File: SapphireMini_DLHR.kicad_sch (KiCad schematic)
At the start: 24 parts, among them IC201 DLHR-F50D-E1BD-C-NAV8, U201 LIS331DLHTR, U202 BMP388

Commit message: Minor changes to annotation
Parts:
- removed R203, R206: 10K, Resistor_SMD:R_0603_1608Metric, symbol Device:R_Small_US
- removed R208, R211: 4K75, Resistor_SMD:R_0603_1608Metric, symbol Device:R_Small_US
- added R209, R210: 47, Resistor_SMD:R_0603_1608Metric, symbol Device:R_Small_US
- renumbered R212 to R203, R207 to R206, R209 to R207, R210 to R208, R213 to R211
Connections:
- net I2C_SCL: now also R209.2; no longer U202.2 (SCK)
- net I2C_SDA: now also R210.2; no longer U202.4 (SDI)
- new net: R209.1, U202.2 (SCK)
- new net: R210.1, U202.4 (SDI)
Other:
- note added: "BMP390 address 0x76"
- note added: "DLHR I2C address 0x29"
- note added: "LIS331DLHTR address 0x12"

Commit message: Footprints complete. Starting layout
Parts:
- C201: MPN CGA5L1X5R1C226M160AC -> CL21A226MAYNNNE; Manufacturer TDK -> Samsung
- C202, C203, C205, C206, C207: MPN CL10B104KA8NNNC -> CL05A104KA5NNNC
- C204: MPN GRM21BR61E106MA73L -> CL21A106KAYNNNE
- FB201: footprint (none) -> Inductor_SMD:L_0201_0603Metric; MPN (none) -> BLM18AG221SN1D
- IC201: Status Trays -> (none)
- U201: footprint LGA-16_3x3x1mm_STM -> SapphineMinimal:LIS331DLHTR
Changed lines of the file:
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@@
       (effects (font (size 1.27 1.27)) hide)
     )
-    (property "MPN" "CL10B104KA8NNNC" (id 5) (at 73.66 67.31 0)
+    (property "MPN" "CL05A104KA5NNNC" (id 5) (at 73.66 67.31 0)
       (effects (font (size 1.27 1.27)) hide)
     )
@@
       (effects (font (size 1.27 1.27)) hide)
     )
-    (property "Description" "0.1 µF ±10% 25V Ceramic Capacitor X7R 0603 (1608 Metric)" (id 15) (at 73.66 67.31 0)
+    (property "Description" "0.1 µF ±10% 25V Ceramic Capacitor X5R 0402 (1005 Metric)" (id 15) (at 73.66 67.31 0)
       (effects (font (size 1.27 1.27)) hide)
     )
@@
       (effects (font (size 1.27 1.27)) hide)
     )
-    (property "MPN" "CL10B104KA8NNNC" (id 5) (at 59.69 67.31 0)
+    (property "MPN" "CL05A104KA5NNNC" (id 5) (at 59.69 67.31 0)
       (effects (font (size 1.27 1.27)) hide)
     )
@@
       (effects (font (size 1.27 1.27)) hide)
     )
-    (property "Description" "0.1 µF ±10% 25V Ceramic Capacitor X7R 0603 (1608 Metric)" (id 15) (at 59.69 67.31 0)
+    (property "Description" "0.1 µF ±10% 25V Ceramic Capacitor X5R 0402 (1005 Metric)" (id 15) (at 59.69 67.31 0)
       (effects (font (size 1.27 1.27)) hide)
     )
@@
       (effects (font (size 1.27 1.27)) hide)
     )
-    (property "MPN" "CGA5L1X5R1C226M160AC" (id 6) (at 46.99 67.31 0)
-      (effects (font (size 1.27 1.27)) hide)
-    )
-    (property "Manufacturer" "TDK" (id 7) (at 46.99 67.31 0)
+    (property "MPN" "CL21A226MAYNNNE" (id 6) (at 46.99 67.31 0)
+      (effects (font (size 1.27 1.27)) hide)
+    )
+    (property "Manufacturer" "Samsung" (id 7) (at 46.99 67.31 0)
       (effects (font (size 1.27 1.27)) hide)
     )
@@
       (effects (font (size 1.27 1.27)) hide)
     )
-    (property "Description" "22 µF ±20% 16V Ceramic Capacitor X5R 1206" (id 16) (at 46.99 67.31 0)
+    (property "Description" "22 µF ±20% 25V Ceramic Capacitor X5R 0805 (2012 Metric)" (id 16) (at 46.99 67.31 0)
       (effects (font (size 1.27 1.27)) hide)
     )
@@
       (effects (font (size 1.27 1.27)) (justify left) hide)
     )
-    (property "Description" "Board Mount Pressure Sensors Low Voltage Digital Pressure Sensor, 0.5 inH2O" (id 4) (at 121.92 59.69 0)
+    (property "Description" "SENSOR PRESSURE 0.5\" H2O 18 BIT" (id 4) (at 121.92 59.69 0)
       (effects (font (size 1.27 1.27)) (justify left) hide)
     )
@@
       (effects (font (size 1.27 1.27)) hide)
     )
-    (property "Status" "Trays" (id 19) (at 92.71 57.15 0)
+    (property "Status" "" (id 19) (at 92.71 57.15 0)
       (effects (font (size 1.27 1.27)) hide)
     )
@@
       (effects (font (size 1.27 1.27)) hide)
     )
-    (property "MPN" "CL10B104KA8NNNC" (id 5) (at 153.67 140.97 0)
+    (property "MPN" "CL05A104KA5NNNC" (id 5) (at 153.67 140.97 0)
       (effects (font (size 1.27 1.27)) hide)
     )
@@
       (effects (font (size 1.27 1.27)) hide)
     )
-    (property "Description" "0.1 µF ±10% 25V Ceramic Capacitor X7R 0603 (1608 Metric)" (id 15) (at 153.67 140.97 0)
+    (property "Description" "0.1 µF ±10% 25V Ceramic Capacitor X5R 0402 (1005 Metric)" (id 15) (at 153.67 140.97 0)
       (effects (font (size 1.27 1.27)) hide)
     )
@@
       (effects (font (size 1.524 1.524)))
     )
-    (property "Footprint" "LGA-16_3x3x1mm_STM" (id 2) (at 95.25 139.954 0)
+    (property "Footprint" "SapphineMinimal:LIS331DLHTR" (id 2) (at 95.25 139.954 0)
       (effects (font (size 1.524 1.524)) hide)
     )
@@
       (effects (font (size 1.27 1.27)) hide)
     )
-    (property "MPN" "GRM21BR61E106MA73L" (id 5) (at 142.24 140.97 0)
+    (property "MPN" "CL21A106KAYNNNE" (id 5) (at 142.24 140.97 0)
       (effects (font (size 1.27 1.27)) hide)
     )
@@
       (effects (font (size 1.27 1.27)) hide)
     )
-    (property "Description" "10 µF ±20% 25V Ceramic Capacitor X5R 0805" (id 8) (at 142.24 140.97 0)
+    (property "Description" "10 µF ±10% 25V Ceramic Capacitor X5R 0805 (2012 Metric)" (id 8) (at 142.24 140.97 0)
       (effects (font (size 1.27 1.27)) hide)
     )
@@
       (effects (font (size 1.27 1.27)) hide)
     )
-    (property "MPN" "CL10B104KA8NNNC" (id 5) (at 228.6 76.2 0)
+    (property "MPN" "CL05A104KA5NNNC" (id 5) (at 228.6 76.2 0)
       (effects (font (size 1.27 1.27)) hide)
     )
@@
       (effects (font (size 1.27 1.27)) hide)
     )
-    (property "Description" "0.1 µF ±10% 25V Ceramic Capacitor X7R 0603 (1608 Metric)" (id 15) (at 228.6 76.2 0)
+    (property "Description" "0.1 µF ±10% 25V Ceramic Capacitor X5R 0402 (1005 Metric)" (id 15) (at 228.6 76.2 0)
       (effects (font (size 1.27 1.27)) hide)
     )
@@
       (effects (font (size 1.27 1.27)) hide)
     )
-    (property "MPN" "CL10B104KA8NNNC" (id 5) (at 236.22 73.66 0)
+    (property "MPN" "CL05A104KA5NNNC" (id 5) (at 236.22 73.66 0)
       (effects (font (size 1.27 1.27)) hide)
     )
@@
       (effects (font (size 1.27 1.27)) hide)
     )
-    (property "Description" "0.1 µF ±10% 25V Ceramic Capacitor X7R 0603 (1608 Metric)" (id 15) (at 236.22 73.66 0)
+    (property "Description" "0.1 µF ±10% 25V Ceramic Capacitor X5R 0402 (1005 Metric)" (id 15) (at 236.22 73.66 0)
       (effects (font (size 1.27 1.27)) hide)
     )
@@
     (property "Reference" "FB201" (id 0) (at 65.9892 53.3486 90))
     (property "Value" "FerriteBead" (id 1) (at 65.9892 55.8855 90))
-    (property "Footprint" "" (id 2) (at 66.04 61.468 90)
+    (property "Footprint" "Inductor_SMD:L_0201_0603Metric" (id 2) (at 66.04 61.468 90)
       (effects (font (size 1.27 1.27)) hide)
     )
@@
       (effects (font (size 1.27 1.27)) hide)
     )
+    (property "Description" "220 Ohms @ 100 MHz 1 Ferrite Bead 0603 (1608 Metric) 500mA 250mOhm" (id 4) (at 66.04 59.69 0)
+      (effects (font (size 1.27 1.27)) hide)
+    )
+    (property "MPN" "BLM18AG221SN1D" (id 5) (at 66.04 59.69 0)
+      (effects (font (size 1.27 1.27)) hide)
+    )

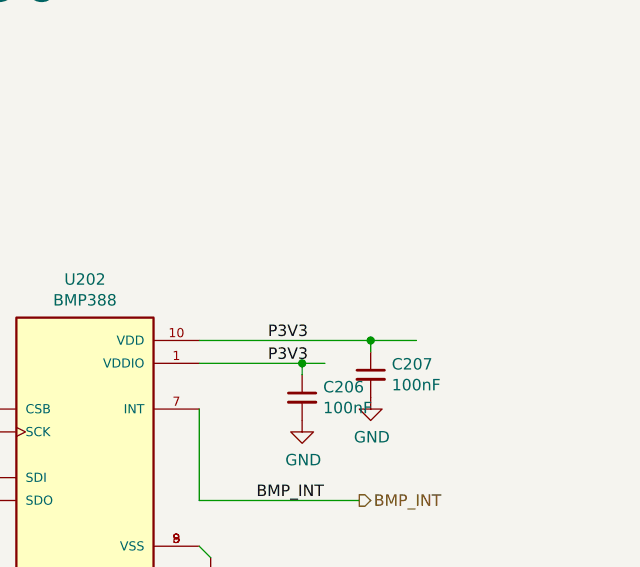
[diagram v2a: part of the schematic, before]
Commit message: replacing w/ resistor array
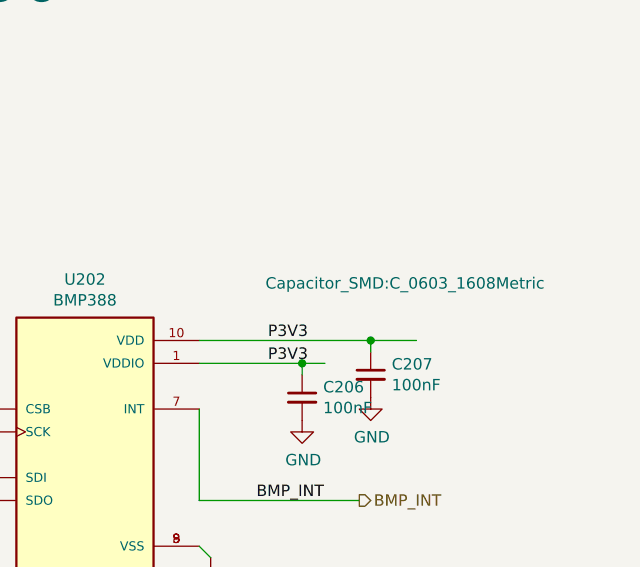
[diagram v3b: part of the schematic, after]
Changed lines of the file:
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@@
       (effects (font (size 1.27 1.27)) (justify left))
     )
-    (property "Footprint" "Capacitor_SMD:C_0603_1608Metric" (id 2) (at 236.22 73.66 0)
-      (effects (font (size 1.27 1.27)) hide)
-    )
+    (property "Footprint" "Capacitor_SMD:C_0603_1608Metric" (id 2) (at 240.03 63.5 0))
     (property "Datasheet" "~" (id 3) (at 236.22 73.66 0)
       (effects (font (size 1.27 1.27)) hide)

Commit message: Checkpoint
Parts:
- removed C204: 10uF, Capacitor_SMD:C_0805_2012Metric, symbol Device:C_Small
- removed C206: 100nF, Capacitor_SMD:C_0603_1608Metric, symbol Device:C_Small
- removed R201, R202, R203, R207, R208, R209, R210: 47, Resistor_SMD:R_0603_1608Metric, symbol Device:R_Small_US
- added R201: EXB-2HV470JV, Sapphire:EXB-2HV470JV, symbol PanasonicRA:EXB-2HV470JV
- U201: footprint SapphineMinimal:LIS331DLHTR -> Sapphire:LIS331DLHTR; DPN 497-10397-1-ND -> (none); Digi-Key_PN 497-10397-1-ND -> (none); Distributor Digikey -> (none); MPN LIS331DLHTR -> (none); Populate 0 -> (none)
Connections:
- net ACC_INT1: now also R201.5
- net ACC_INT2: now also R201.4
- net GND: now also R201.2
- net I2C_SCL: now also R201.1, R201.6
- net I2C_SDA: now also R201.3, R201.7
- net at U201.6 (SDA/SDI/SDO): now also R201.14
- net at U201.4 (SCL/SPC): now also R201.16
- net at U201.11 (INT1): now also R201.12
- net at U201.7 (SDO/SA0): now also R201.15
- net at U201.9 (INT2): now also R201.13
- net BMP_SCK: now reaches U202.2 (SCK)
- net BMP_SCK: now also R201.11
- net BMP_SDI: now reaches U202.4 (SDI)
- net BMP_SDI: now also R201.10
- no-connect marks 2 -> 4
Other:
- moved on the sheet: C205, R206

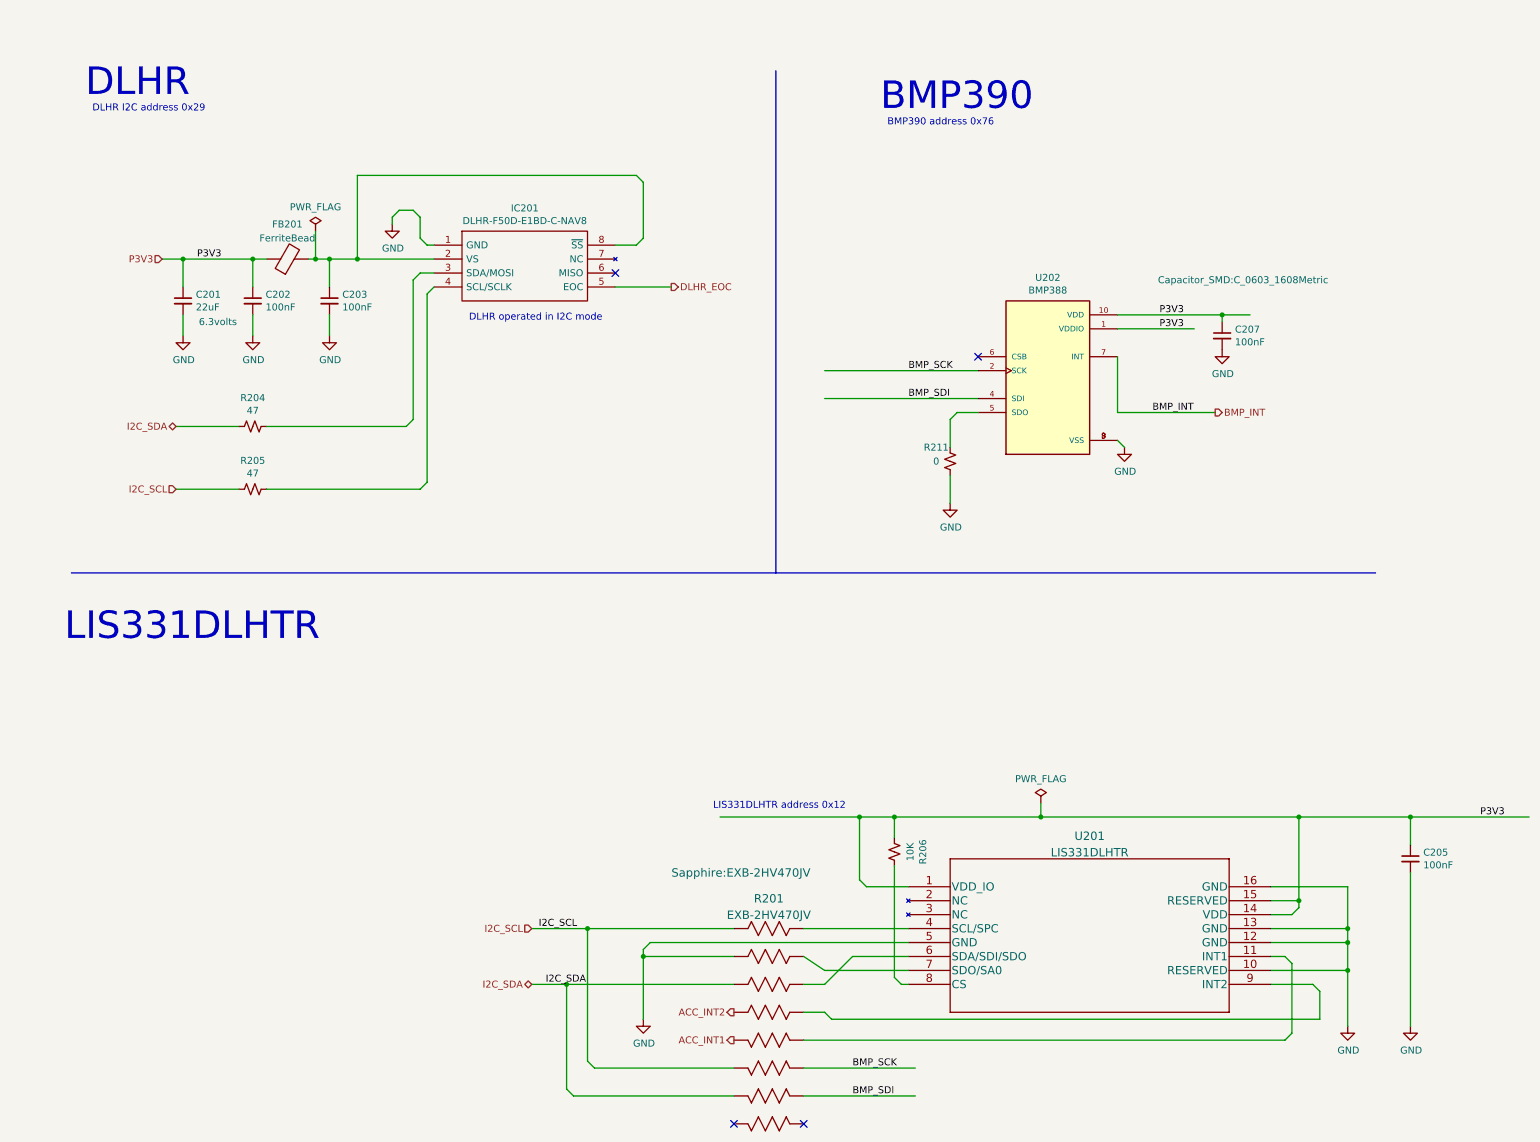
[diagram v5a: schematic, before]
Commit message: Updating for parts avail
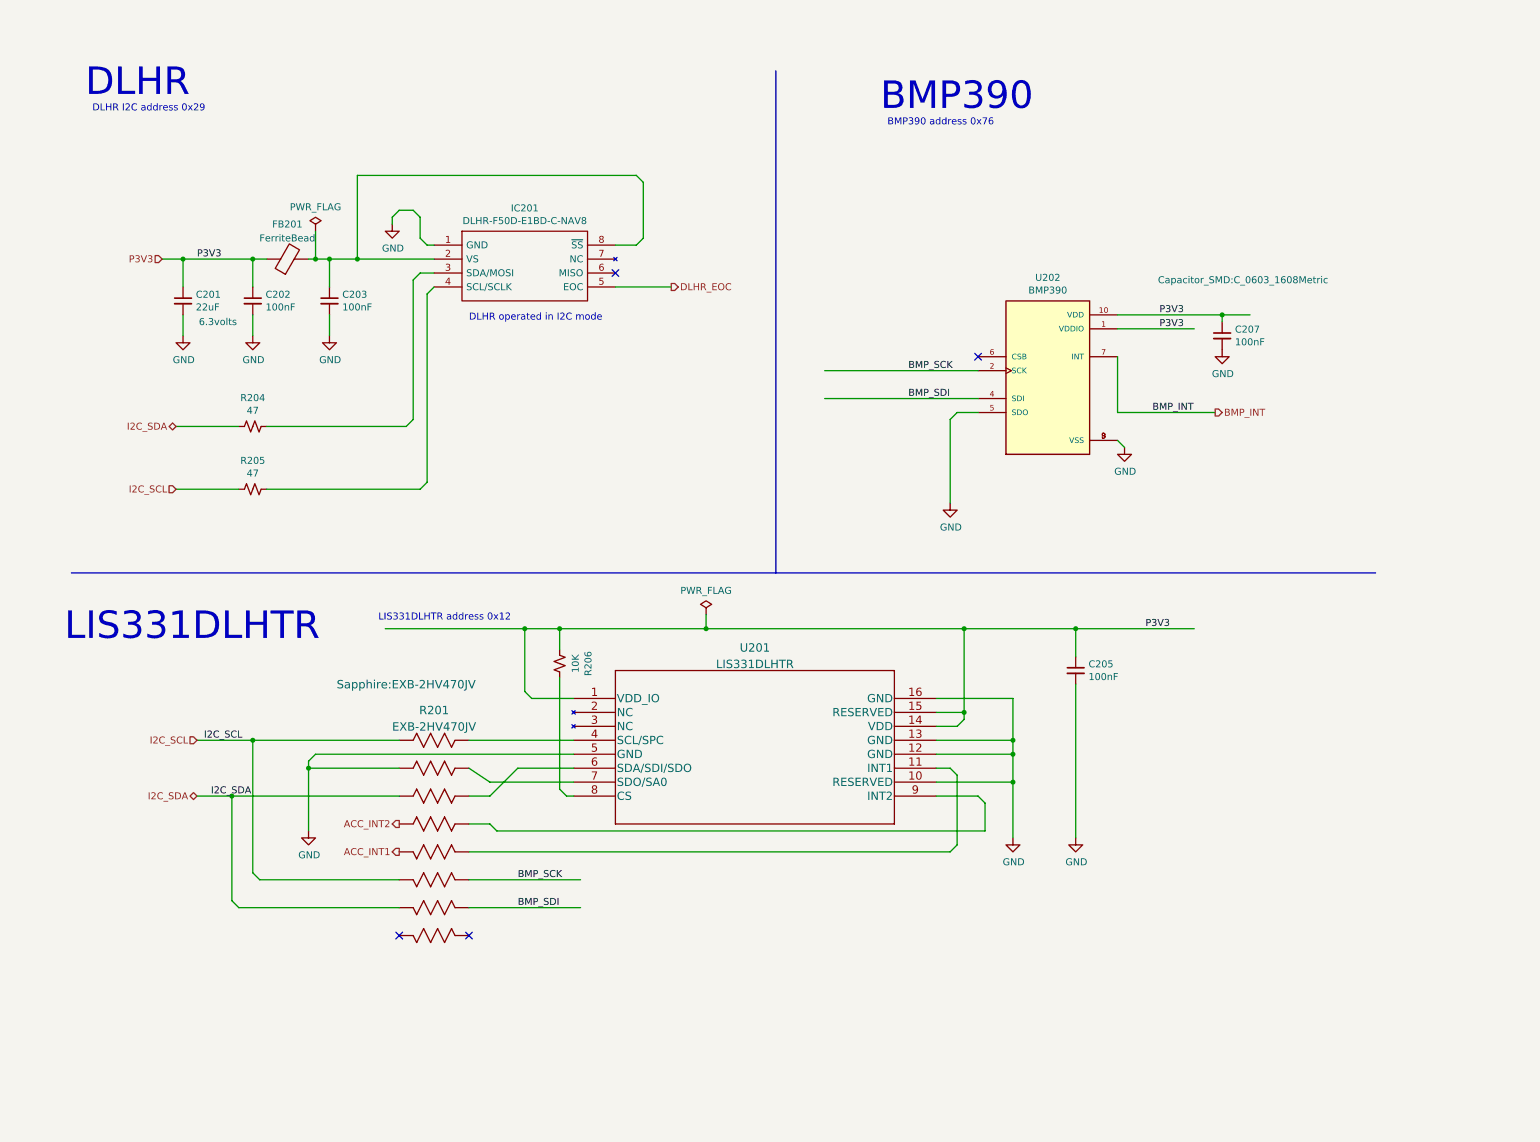
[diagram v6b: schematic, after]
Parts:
- removed R211: 0, Resistor_SMD:R_0603_1608Metric, symbol Device:R_Small_US
- U202: value BMP388 -> BMP390; MPN BMP388 -> BMP390
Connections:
- net GND: now also U202.5 (SDO)
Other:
- moved on the sheet: C205, R201, R206, U201

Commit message: Skematic updated for power and 1PSI sensor
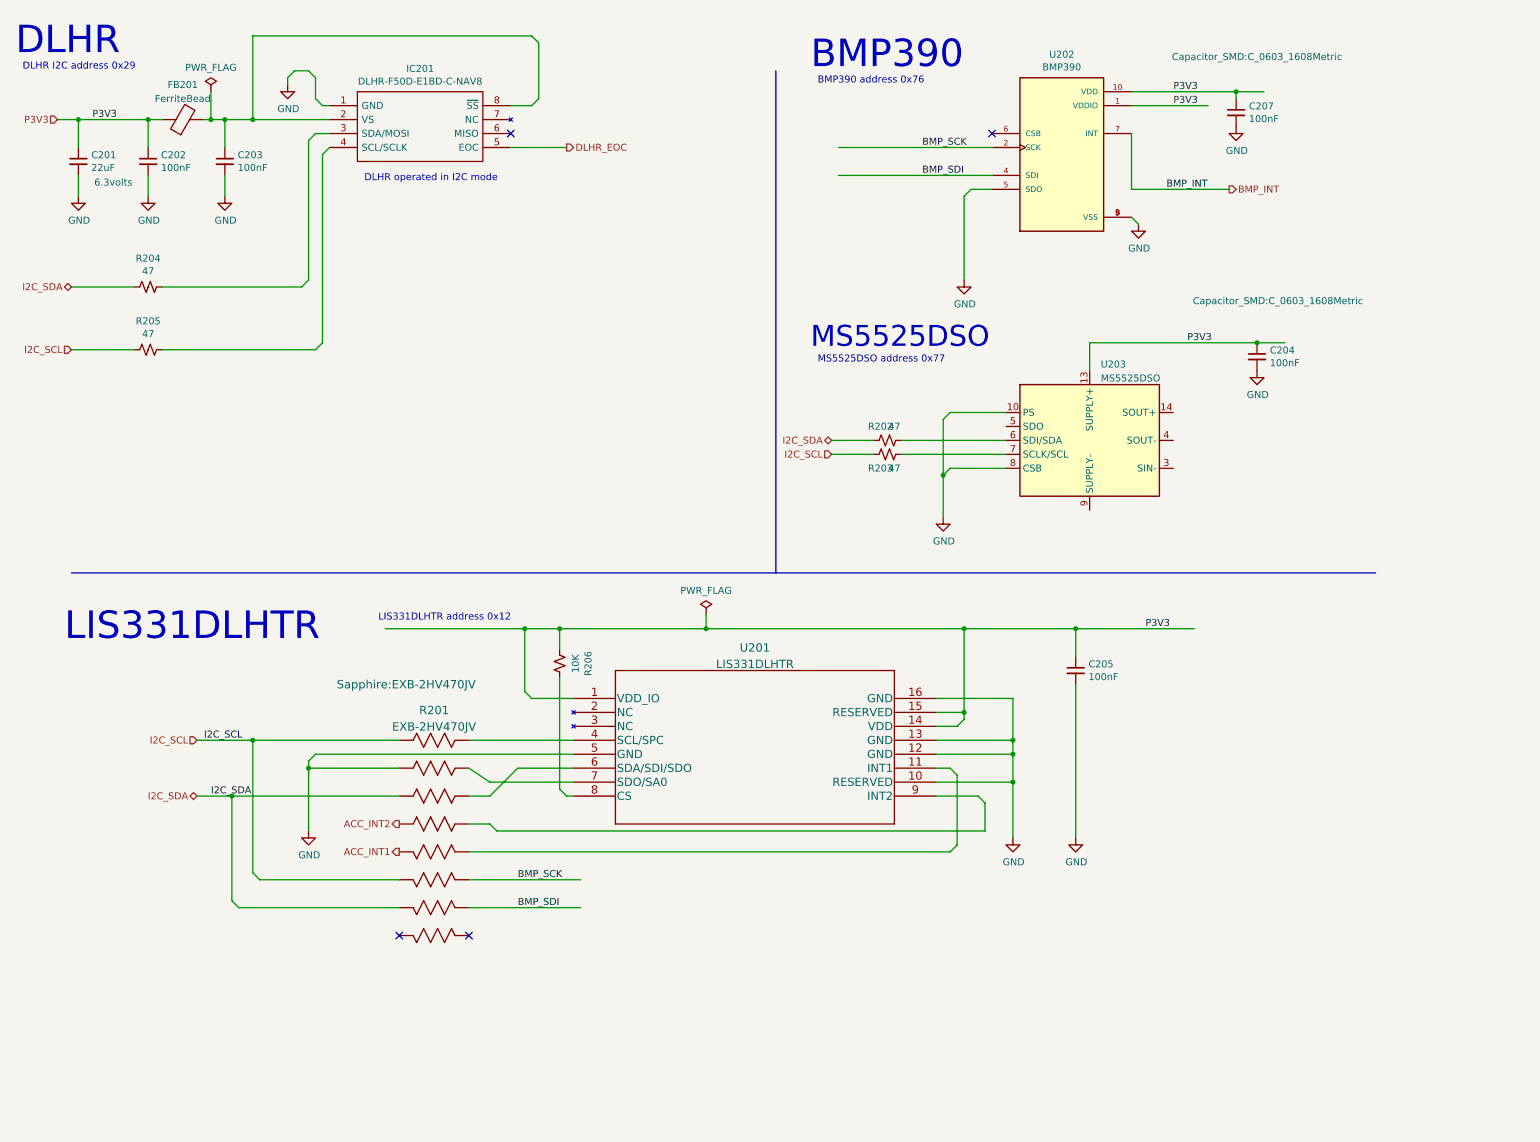
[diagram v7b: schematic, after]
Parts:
- added C204: 100nF, Capacitor_SMD:C_0603_1608Metric, symbol Device:C_Small
- added R202, R203: 47, Resistor_SMD:R_0603_1608Metric, symbol Device:R_Small_US
- added U203: MS5525DSO, SapphineMinimal:TE_MS5525DSO-DBxxxyS, symbol Sensor_Pressure:MS5525DSO
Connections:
- net GND: now also C204.2, U203.10 (PS), U203.8 (CSB)
- net I2C_SCL: now also R203.2
- net I2C_SDA: now also R202.2
- net P3V3: now also C204.1, U203.11 (SUPPLY+), U203.13 (SUPPLY+)
- new net: R202.1, U203.6 (SDI/SDA)
- new net: U203.1 (SIN-), U203.3 (SIN-)
- new net: U203.12 (SOUT+), U203.14 (SOUT+)
- new net: U203.2 (SOUT-), U203.4 (SOUT-)
- new net: R203.1, U203.7 (SCLK/SCL)
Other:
- note added: "MS5525DSO"
- note added: "MS5525DSO address 0x77"
- moved on the sheet: C201, C202, C203, C207, FB201, IC201, R204, R205, U202
